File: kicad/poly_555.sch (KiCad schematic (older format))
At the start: 24 parts, among them U1 LM386

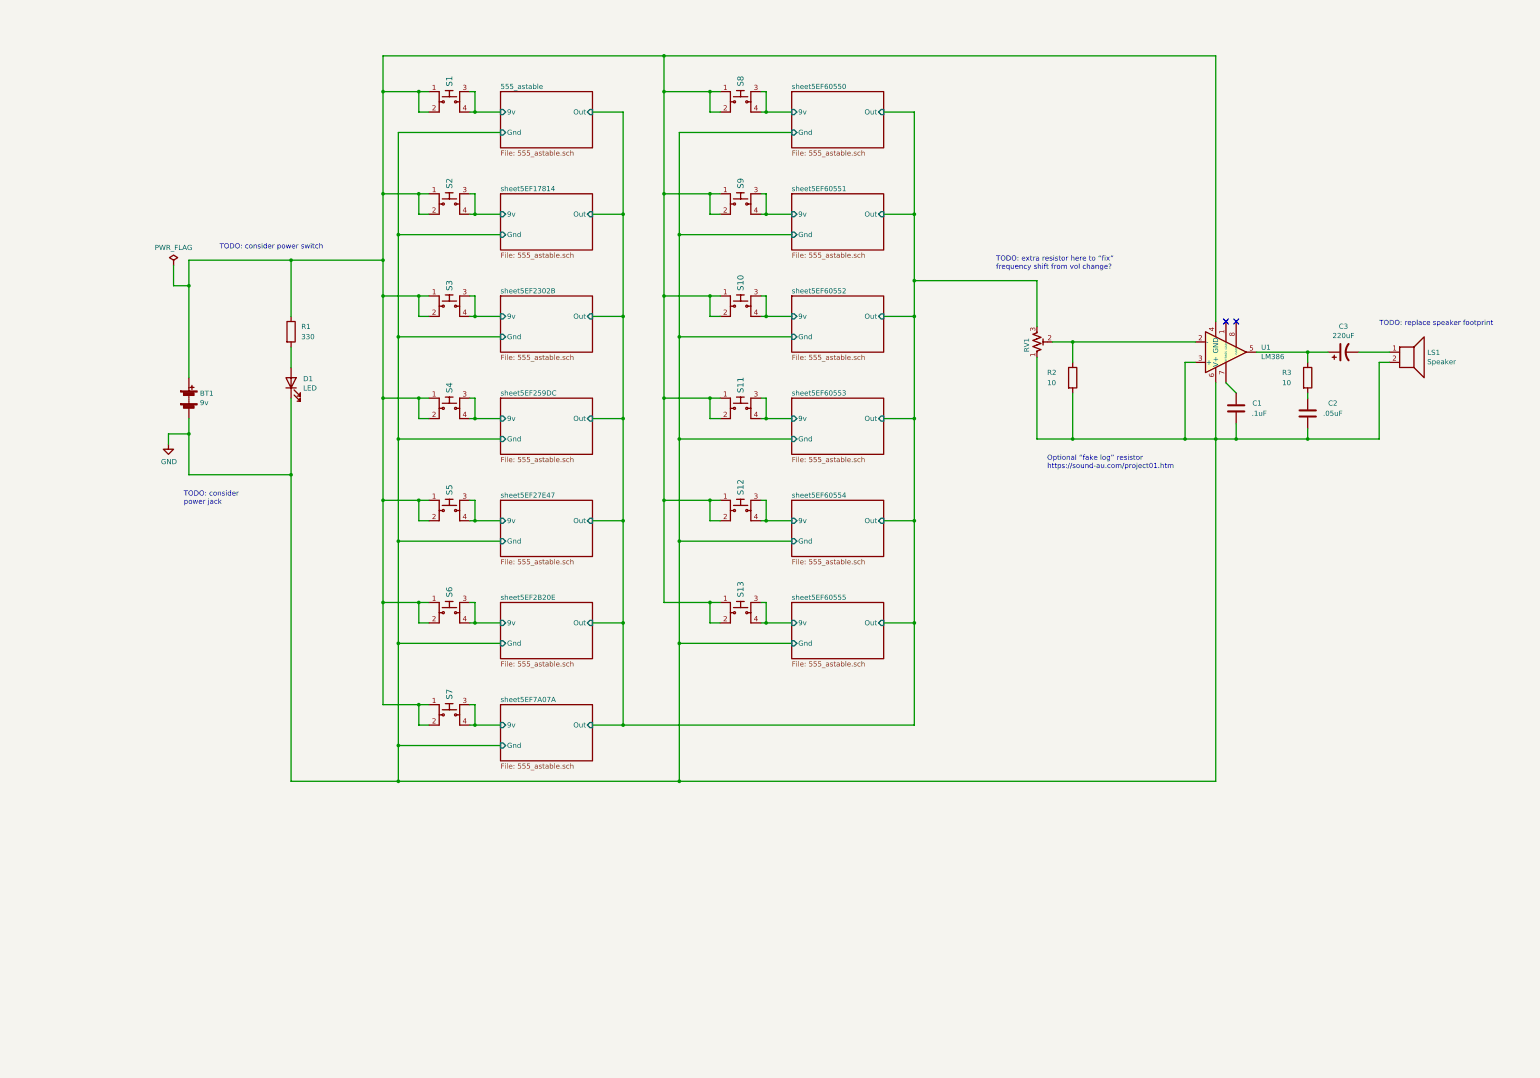
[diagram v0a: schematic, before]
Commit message: Schematic: add switch, more 555s, update TODOs
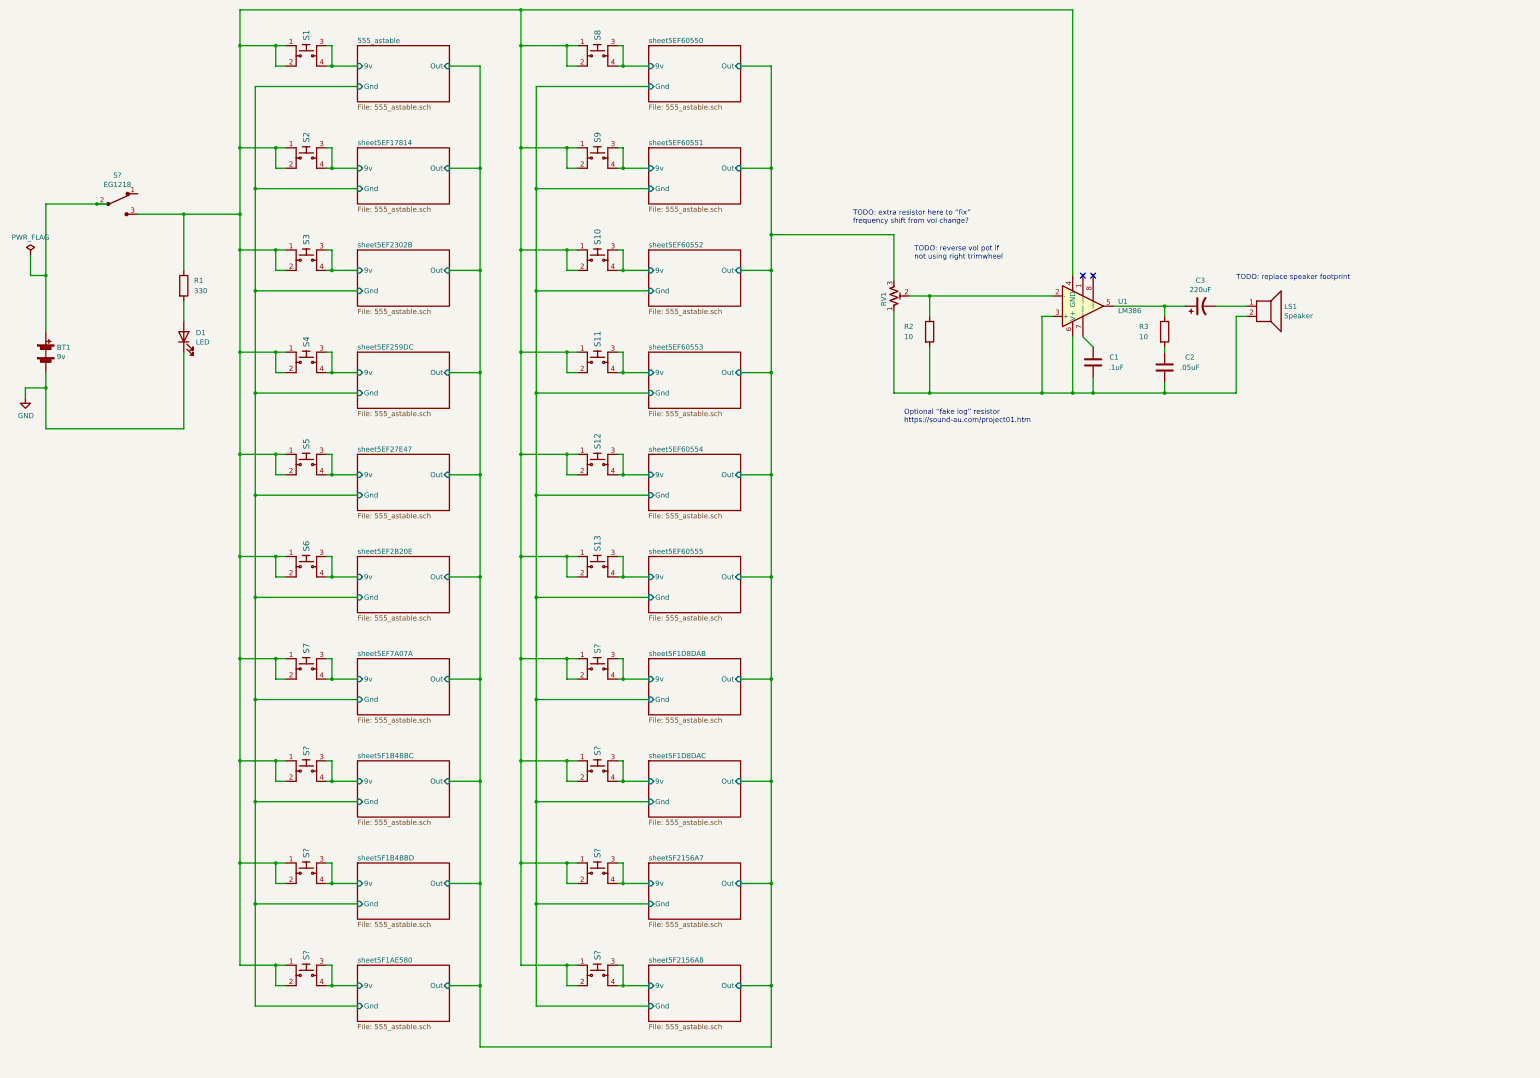
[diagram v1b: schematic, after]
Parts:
- added S? (x7): FSM4JSMATR, Button_Switch_THT:SW_TH_Tactile_Omron_B3F-10xx, symbol dk_Tactile-Switches:FSM4JSMATR
- added S?: EG1218, digikey-footprints:Switch_Slide_11.6x4mm_EG1218, symbol dk_Slide-Switches:EG1218
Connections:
- net GND: no longer C1.1, C2.2, LS1.2, R2.2, RV1.1, U1.3 (+), U1.6 (V+)
- net at R1.1, S1.1, S1.2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: now also S?.1, S?.1, S?.1, S?.1, S?.1, S?.1, S?.1, S?.2, S?.2, S?.2, S?.2, S?.2, S?.2, S?.2, S?.3; no longer BT1.1 (+)
- new net: BT1.1 (+), S?.2
- new net: C1.1, C2.2, LS1.2, R2.2, RV1.1, U1.3 (+), U1.6 (V+)
- new net sheet5F1AE580/9v: S?.3, S?.4
- new net sheet5F1B4BBC/9v: S?.3, S?.4
- new net sheet5F1B4BBD/9v: S?.3, S?.4
- new net sheet5F1D8DAB/9v: S?.3, S?.4
- new net sheet5F1D8DAC/9v: S?.3, S?.4
- new net sheet5F2156A7/9v: S?.3, S?.4
- new net sheet5F2156A8/9v: S?.3, S?.4
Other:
- note added: "TODO: reverse vol pot if\nnot using right trimwheel"
- note removed: "TODO: consider power switch"
- note removed: "TODO: consider\npower jack"
- moved on the sheet: BT1, C1, C2, C3, D1, LS1, R1, R2, R3, RV1, S1, S10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

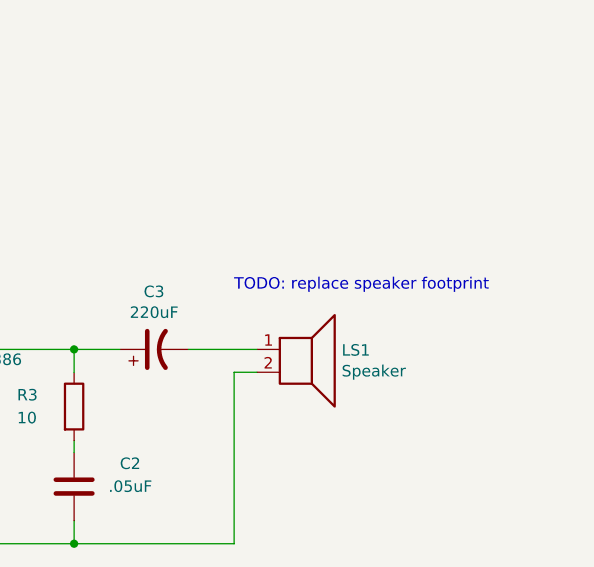
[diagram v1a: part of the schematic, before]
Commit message: Reverse fine tuning rotation
These pots are countinerintuitive
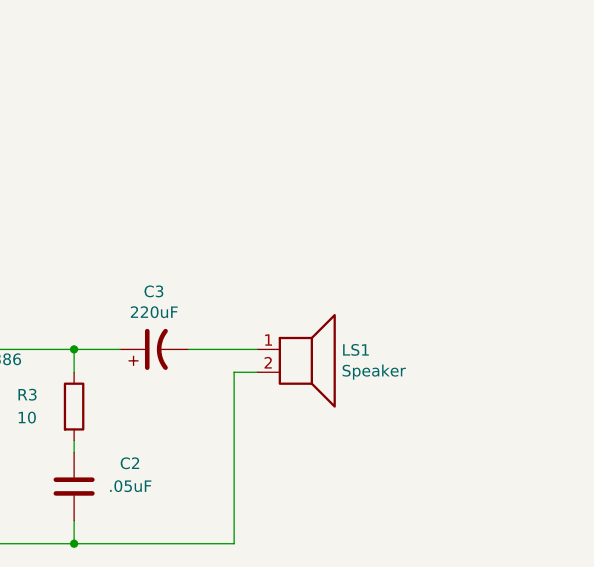
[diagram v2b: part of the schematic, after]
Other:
- note removed: "TODO: replace speaker footprint"
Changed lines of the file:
@@
 	12150 3600 12350 3600
 Connection ~ 12150 3600
-$Comp
-L Device:Speaker LS1
-U 1 1 5F32F818
-P 13150 3600
-F 0 "LS1" H 13320 3596 50  0000 L CNN
-F 1 "Speaker" H 13320 3505 50  0000 L CNN
-F 2 "Connector_PinHeader_2.54mm:PinHeader_1x02_P2.54mm_Vertical" H 13150 3400 50  0001 C CNN
-F 3 "~" H 13140 3550 50  0001 C CNN
-	1    13150 3600
-	1    0    0    -1
-$EndComp
 Wire Wire Line
 	12650 3600 12950 3600
@@
 Wire Wire Line
 	1200 4400 1200 4800
-Text Notes 12850 3350 0    50   ~ 0
-TODO: replace speaker footprint
 Wire Wire Line
 	5450 1250 5450 2250
@@
 	2100 2700 2550 2700
 Connection ~ 2550 2700
+$Comp
+L Device:Speaker LS1
+U 1 1 5F32F818
+P 13150 3600
+F 0 "LS1" H 13320 3596 50  0000 L CNN
+F 1 "Speaker" H 13320 3505 50  0000 L CNN
+F 2 "Connector_PinHeader_2.54mm:PinHeader_1x02_P2.54mm_Vertical" H 13150 3400 50  0001 C CNN
+F 3 "~" H 13140 3550 50  0001 C CNN
+	1    13150 3600
+	1    0    0    -1
+$EndComp
 $EndSCHEMATC

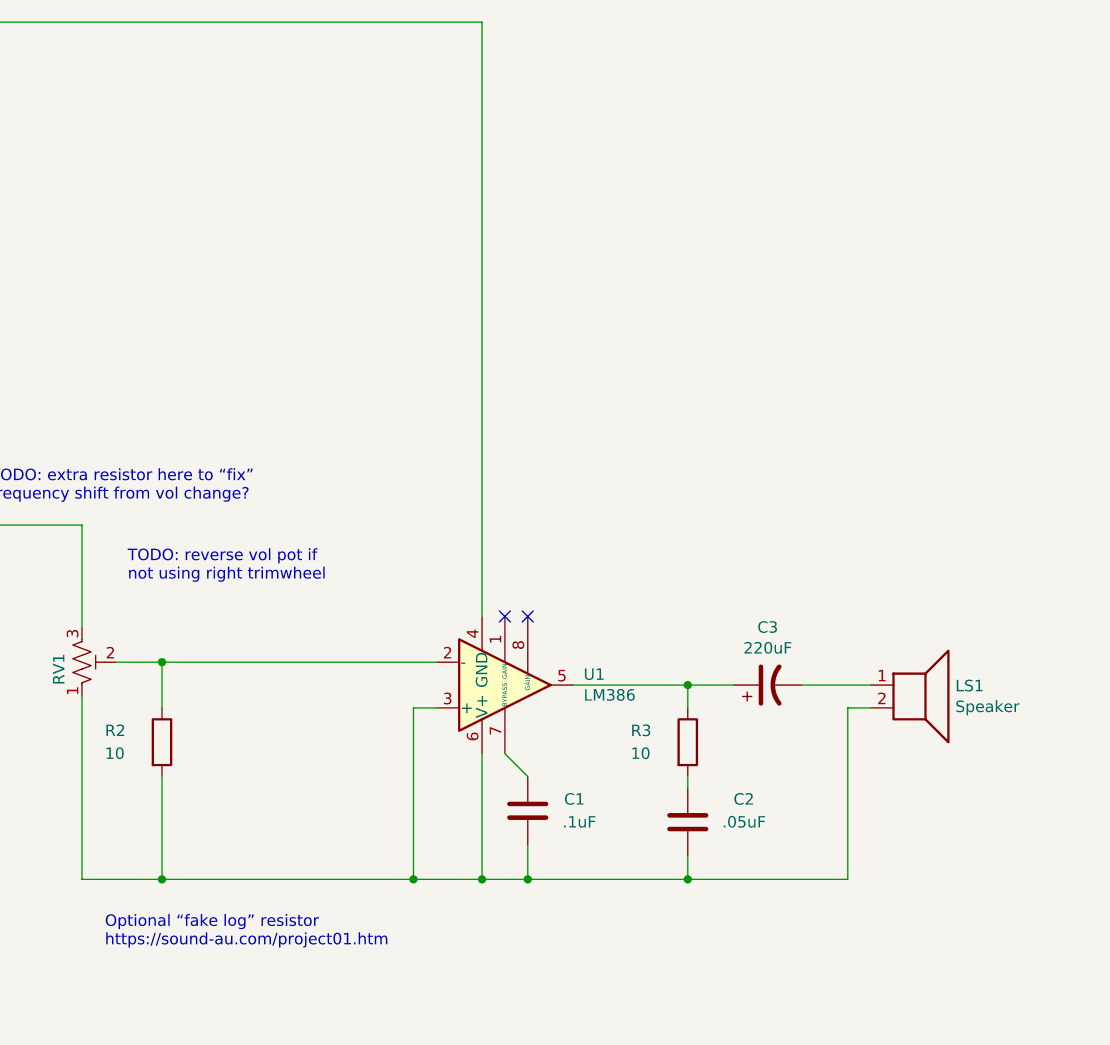
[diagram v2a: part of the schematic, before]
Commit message: Fix swapped 386 POW/GND pins
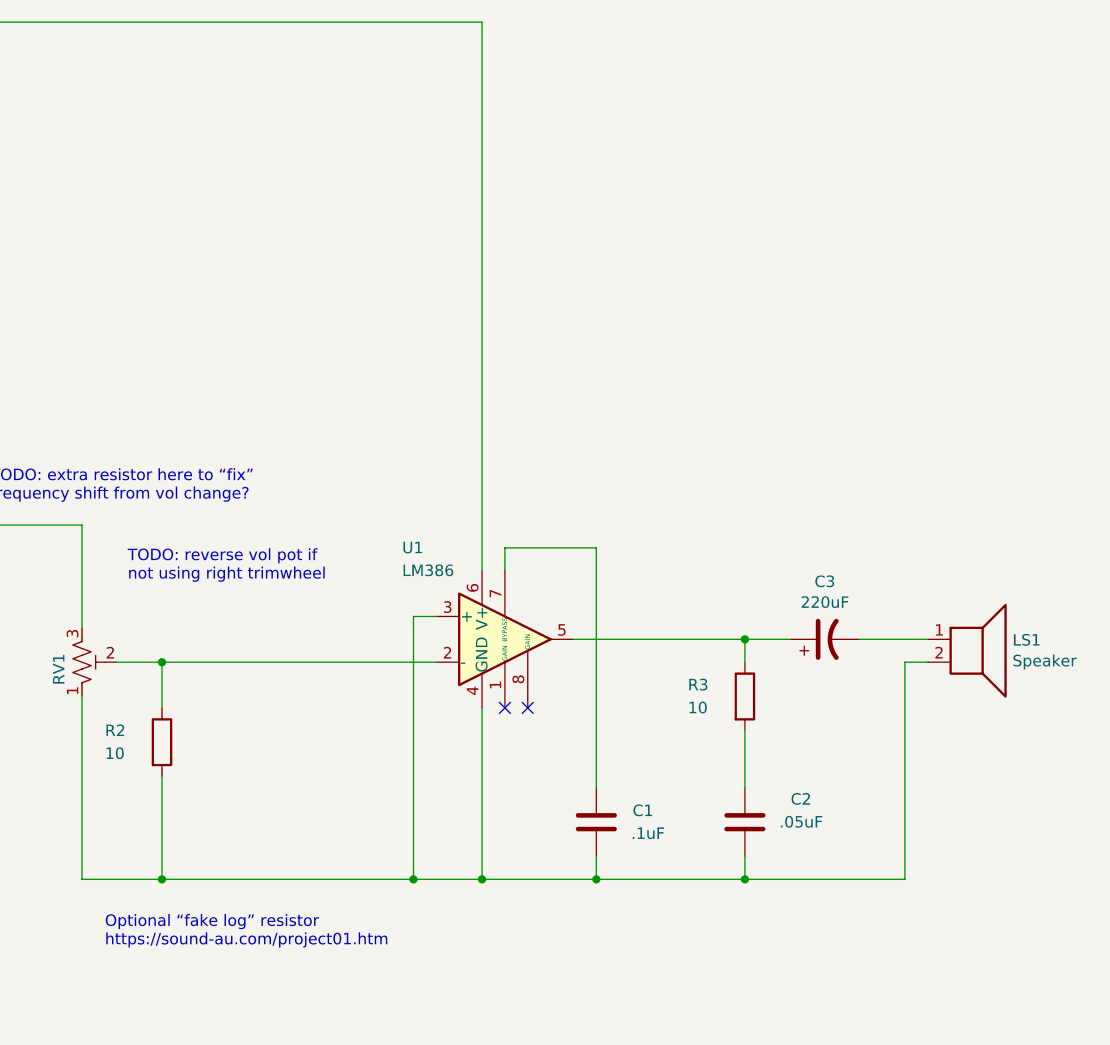
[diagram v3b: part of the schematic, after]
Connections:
- net at R1.1, S1.1, S1.2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: now also U1.6 (V+); no longer U1.4 (GND)
- net at C1.1, C2.2, LS1.2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: now also U1.4 (GND); no longer U1.6 (V+)
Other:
- moved on the sheet: C1, C2, C3, LS1, R3, U1

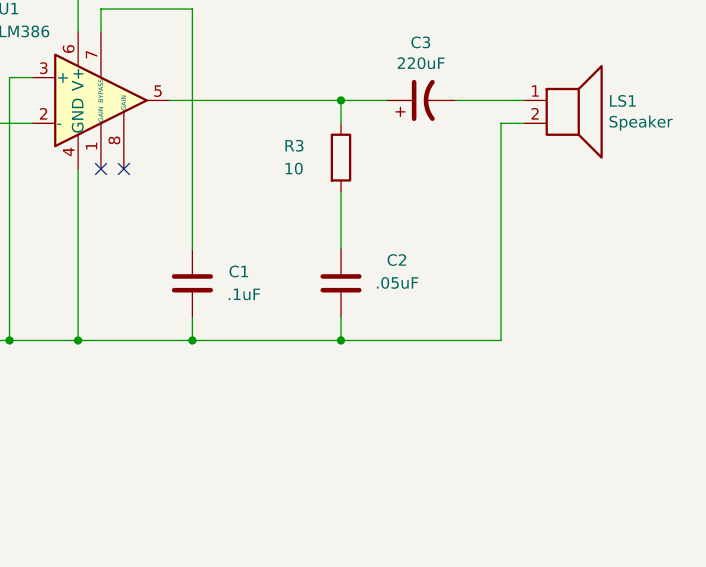
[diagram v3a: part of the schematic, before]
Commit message: Update 386 shunt cap to on hand stock
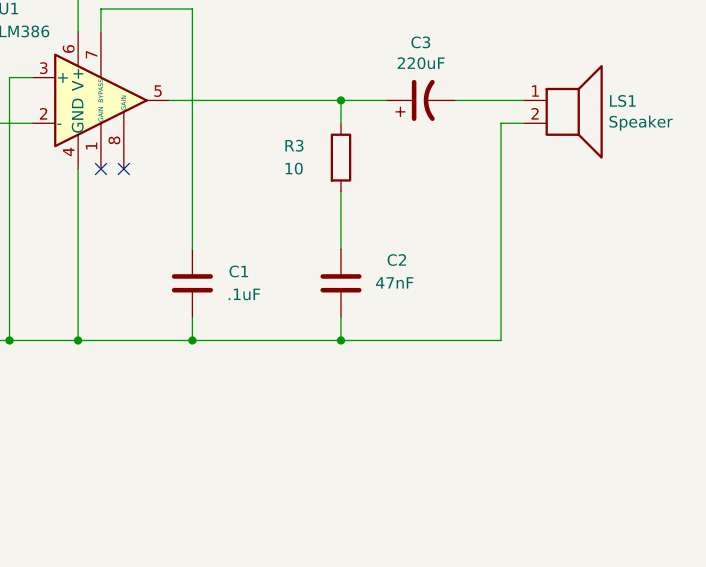
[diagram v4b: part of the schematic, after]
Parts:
- C2: value .05uF -> 47nF
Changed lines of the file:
@@
 AR Path="/5EF7A07F/5F234E50" Ref="C?"  Part="1"
 F 0 "C2" H 12600 4300 50  0000 L CNN
-F 1 ".05uF" H 12550 4200 50  0000 L CNN
+F 1 "47nF" H 12550 4200 50  0000 L CNN
 F 2 "Capacitor_THT:C_Disc_D5.0mm_W2.5mm_P5.00mm" H 12438 4050 50  0001 C CNN
 F 3 "~" H 12400 4200 50  0001 C CNN

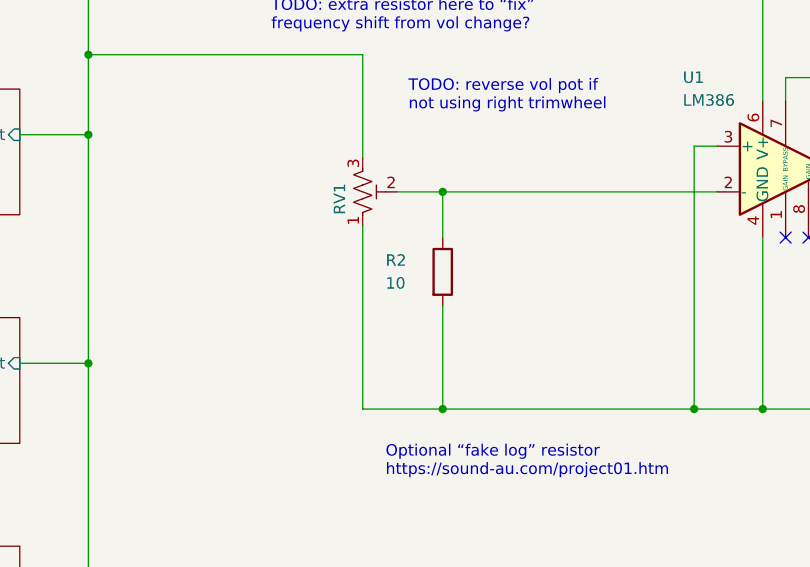
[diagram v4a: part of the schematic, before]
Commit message: Update values: timing cap, tuning pots, log resistor
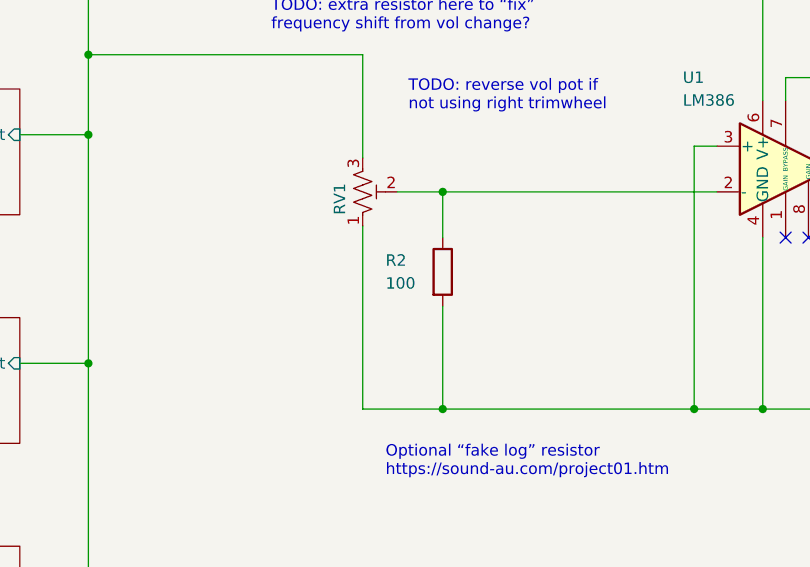
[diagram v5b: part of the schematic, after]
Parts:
- R2: value 10 -> 100
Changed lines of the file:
@@
 AR Path="/60F96869/5F3FF342" Ref="R?"  Part="1"
 F 0 "R2" H 9600 3900 50  0000 L CNN
-F 1 "10" H 9600 3800 50  0000 L CNN
+F 1 "100" H 9600 3800 50  0000 L CNN
 F 2 "Resistor_THT:R_Axial_DIN0204_L3.6mm_D1.6mm_P7.62mm_Horizontal" V 9780 3850 50  0001 C CNN
 F 3 "~" H 9850 3850 50  0001 C CNN
